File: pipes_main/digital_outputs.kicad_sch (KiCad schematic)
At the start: 56 parts, among them J13 3.5mm Jack, J14 3.5mm Jack, J15 3.5mm Jack, J16 3.5mm Jack, J17 3.5mm Jack, J18 3.5mm Jack, J19 3.5mm Jack, J20 3.5mm Jack, U36 CD40107, U37 CD40107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

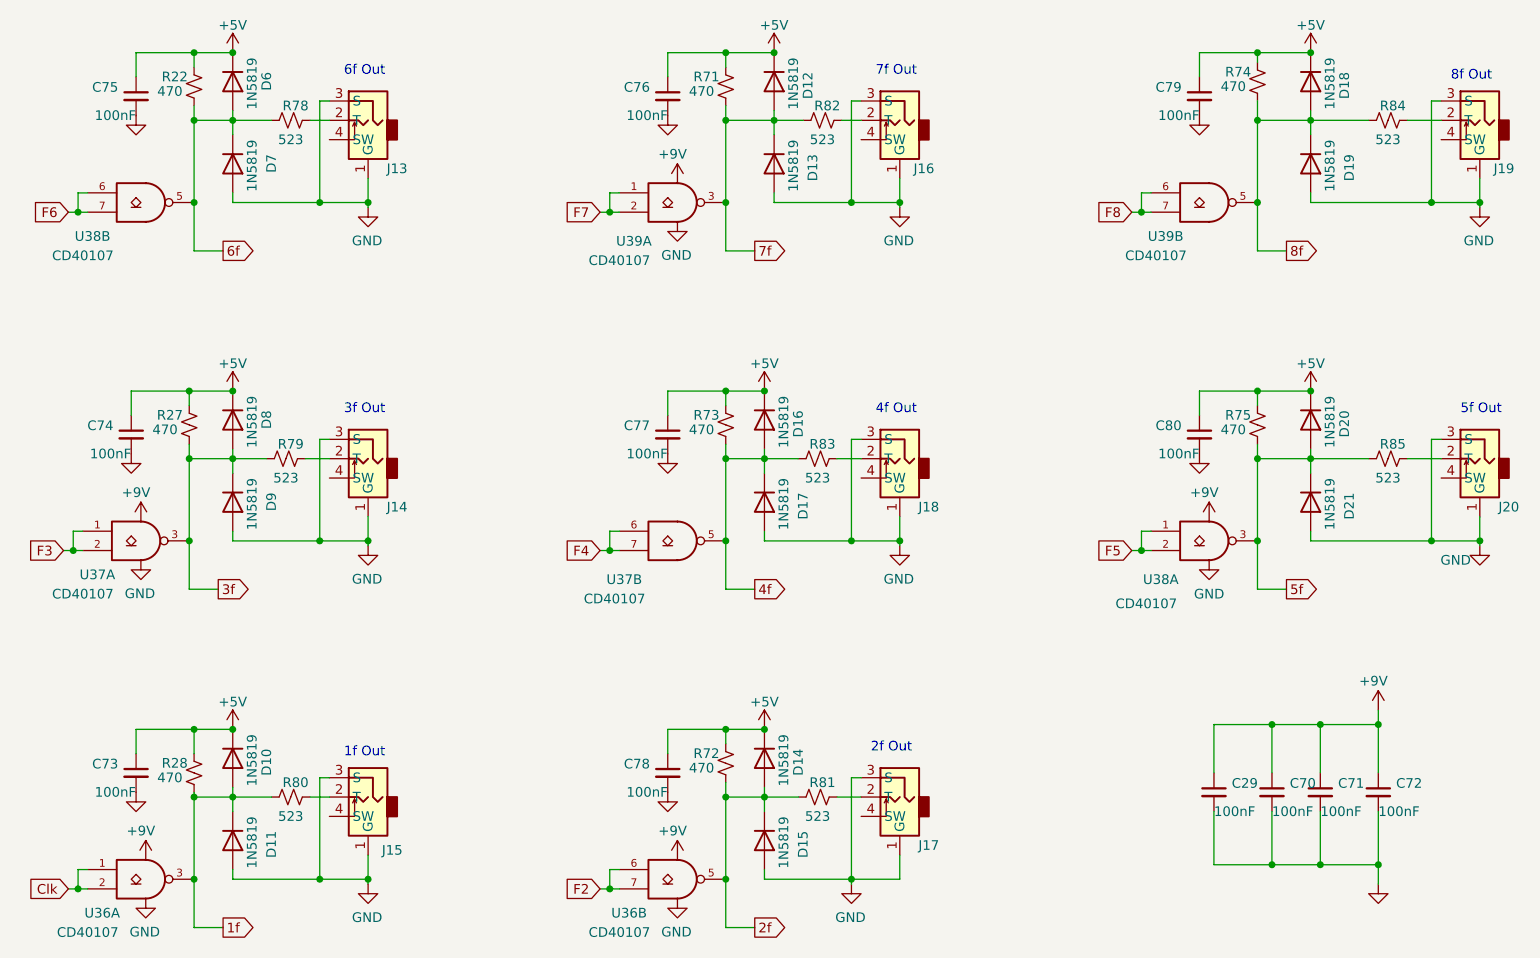
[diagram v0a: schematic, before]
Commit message: Updates component values. Uses .5W resistors on outputs now.
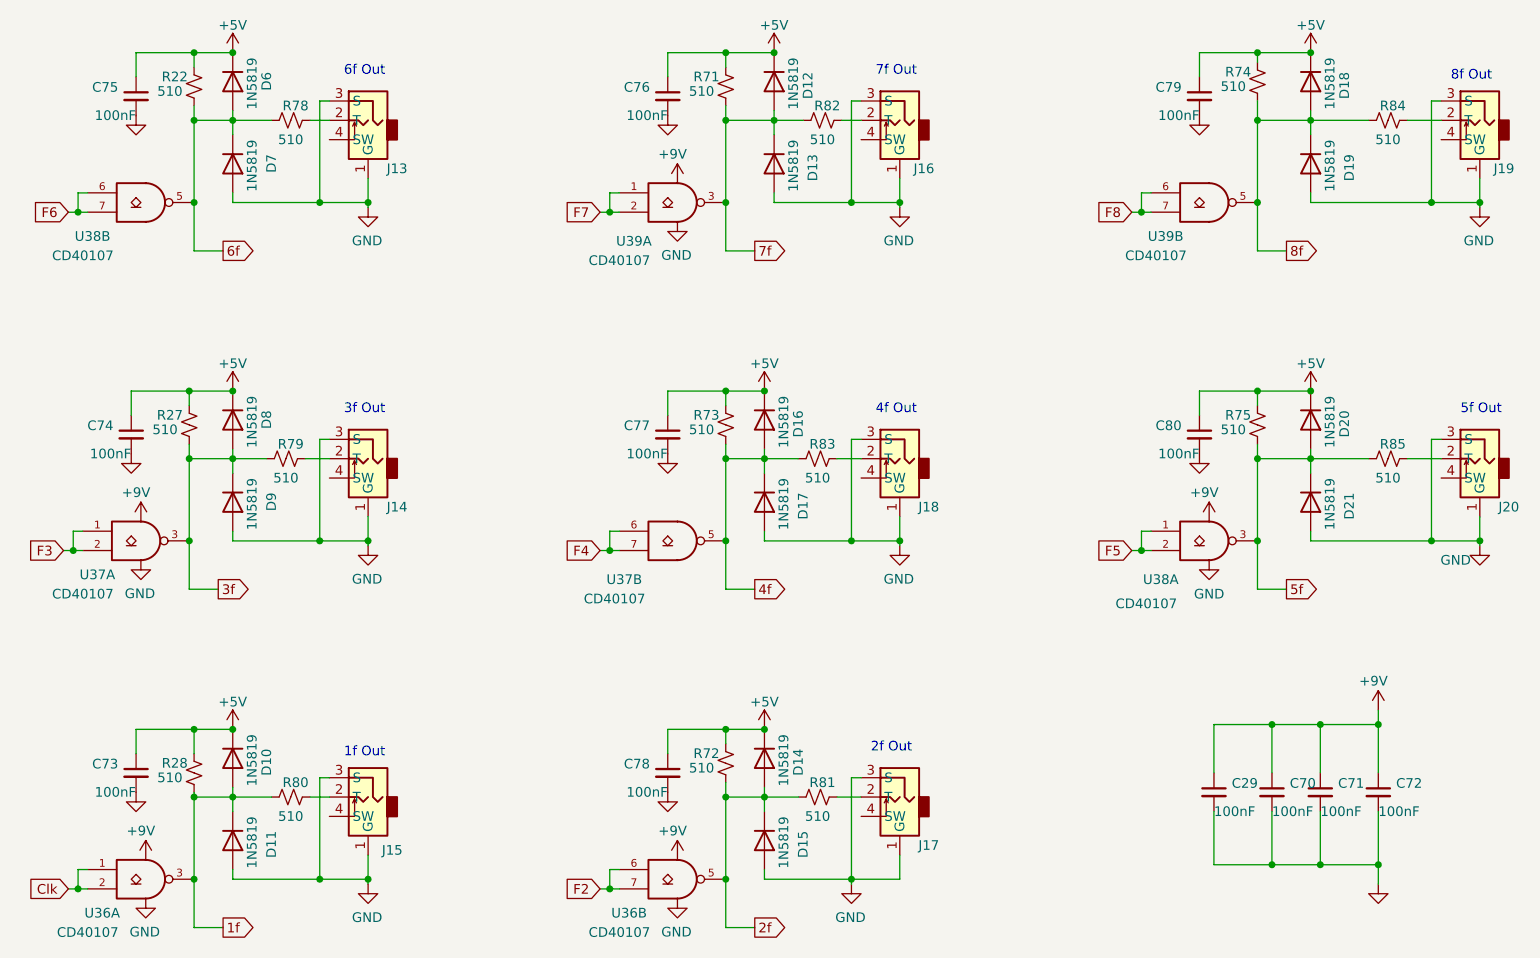
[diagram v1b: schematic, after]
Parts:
- R22, R27, R28, R71, R72, R73, R74, R75: value 470 -> 510; LCSC Part # C17710 -> C2842425
- R78, R79, R80, R81, R82, R83, R84, R85: value 523 -> 510; footprint Resistor_SMD:R_0603_1608Metric -> Resistor_SMD:R_0805_2012Metric_Pad1.20x1.40mm_HandSolder; LCSC Part # C227952 -> C2842425

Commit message: Version 1.1 of boards
Changes to use NSL-32SR3 Vactrols
Fixes 3904 package
Adds 10-step waveform
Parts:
- U36, U37, U38, U39: Digi-Key Part (none) -> 296-31481-1-ND; LCSC Part # (none) -> C2691402
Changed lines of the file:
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@@
+      (effects (font (size 1.27 1.27)) hide)
+    )
+    (property "LCSC Part #" "C2691402" (id 4) (at 46.355 114.3 0)
+      (effects (font (size 1.27 1.27)) hide)
+    )
+    (property "Digi-Key Part" "296-31481-1-ND" (id 5) (at 46.355 114.3 0)
       (effects (font (size 1.27 1.27)) hide)
     )
@@
     )
     (property "Datasheet" "http://www.ti.com/lit/sg/scyt129e/scyt129e.pdf" (id 3) (at 116.8908 166.3192 0)
+      (effects (font (size 1.27 1.27)) hide)
+    )
+    (property "LCSC Part #" "C2691402" (id 4) (at 116.84 158.75 0)
+      (effects (font (size 1.27 1.27)) hide)
+    )
+    (property "Digi-Key Part" "296-31481-1-ND" (id 5) (at 116.84 158.75 0)
       (effects (font (size 1.27 1.27)) hide)
     )
@@
       (effects (font (size 1.27 1.27)) hide)
     )
+    (property "LCSC Part #" "C2691402" (id 4) (at 46.99 158.75 0)
+      (effects (font (size 1.27 1.27)) hide)
+    )
+    (property "Digi-Key Part" "296-31481-1-ND" (id 5) (at 46.99 158.75 0)
+      (effects (font (size 1.27 1.27)) hide)
+    )
     (pin "4")
     (pin "8")
@@
     )
     (property "Datasheet" "http://www.ti.com/lit/sg/scyt129e/scyt129e.pdf" (id 3) (at 116.8908 121.8692 0)
+      (effects (font (size 1.27 1.27)) hide)
+    )
+    (property "LCSC Part #" "C2691402" (id 4) (at 116.84 114.3 0)
+      (effects (font (size 1.27 1.27)) hide)
+    )
+    (property "Digi-Key Part" "296-31481-1-ND" (id 5) (at 116.84 114.3 0)
       (effects (font (size 1.27 1.27)) hide)
     )
@@
       (effects (font (size 1.27 1.27)) hide)
     )
+    (property "LCSC Part #" "C2691402" (id 4) (at 116.84 69.85 0)
+      (effects (font (size 1.27 1.27)) hide)
+    )
+    (property "Digi-Key Part" "296-31481-1-ND" (id 5) (at 116.84 69.85 0)
+      (effects (font (size 1.27 1.27)) hide)
+    )
     (pin "4")
     (pin "8")
@@
     )
     (property "Datasheet" "http://www.ti.com/lit/sg/scyt129e/scyt129e.pdf" (id 3) (at 186.7408 77.4192 0)
+      (effects (font (size 1.27 1.27)) hide)
+    )
+    (property "LCSC Part #" "C2691402" (id 4) (at 186.69 69.85 0)
+      (effects (font (size 1.27 1.27)) hide)
+    )
+    (property "Digi-Key Part" "296-31481-1-ND" (id 5) (at 186.69 69.85 0)
       (effects (font (size 1.27 1.27)) hide)
     )
@@
       (effects (font (size 1.27 1.27)) hide)
     )
+    (property "LCSC Part #" "C2691402" (id 4) (at 46.99 69.85 0)
+      (effects (font (size 1.27 1.27)) hide)
+    )
+    (property "Digi-Key Part" "296-31481-1-ND" (id 5) (at 46.99 69.85 0)
+      (effects (font (size 1.27 1.27)) hide)
+    )
     (pin "4")
     (pin "8")
@@
       (effects (font (size 1.27 1.27)) hide)
     )
+    (property "LCSC Part #" "C2691402" (id 4) (at 186.69 114.3 0)
+      (effects (font (size 1.27 1.27)) hide)
+    )
+    (property "Digi-Key Part" "296-31481-1-ND" (id 5) (at 186.69 114.3 0)
+      (effects (font (size 1.27 1.27)) hide)
+    )
